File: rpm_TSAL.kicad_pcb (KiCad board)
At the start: 2 copper layers, 75.6 x 66.3 mm, 7 parts, among them J1 Conn_01x02, J2 Conn_01x02, J3 Conn_01x02, J4 Conn_01x02, U1 ADUM5202WCRWZ, U2 ADUM5202WCRWZ

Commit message: Saved. Initial Structure done.
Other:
- board size 75.6 x 66.3 mm -> 75.6 x 85 mm
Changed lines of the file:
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@@
 	(gr_rect
 		(start 47.425 59.325)
-		(end 123.025 125.625)
+		(end 123.025 144.325)
 		(stroke
 			(width 0.05)

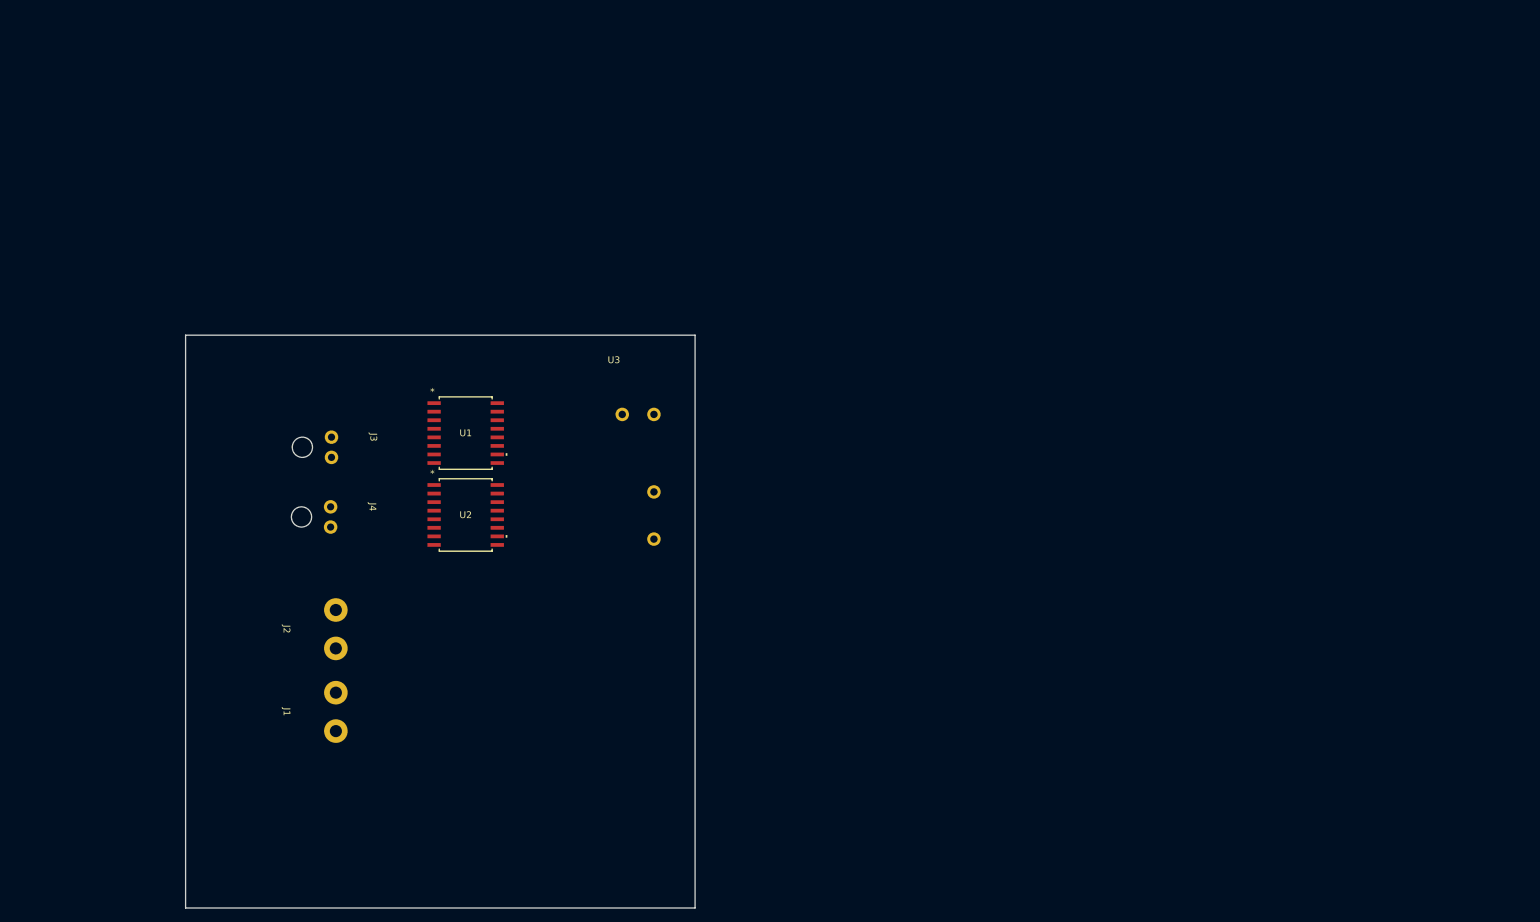
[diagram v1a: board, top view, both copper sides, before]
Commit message: Changes to Pinout pending
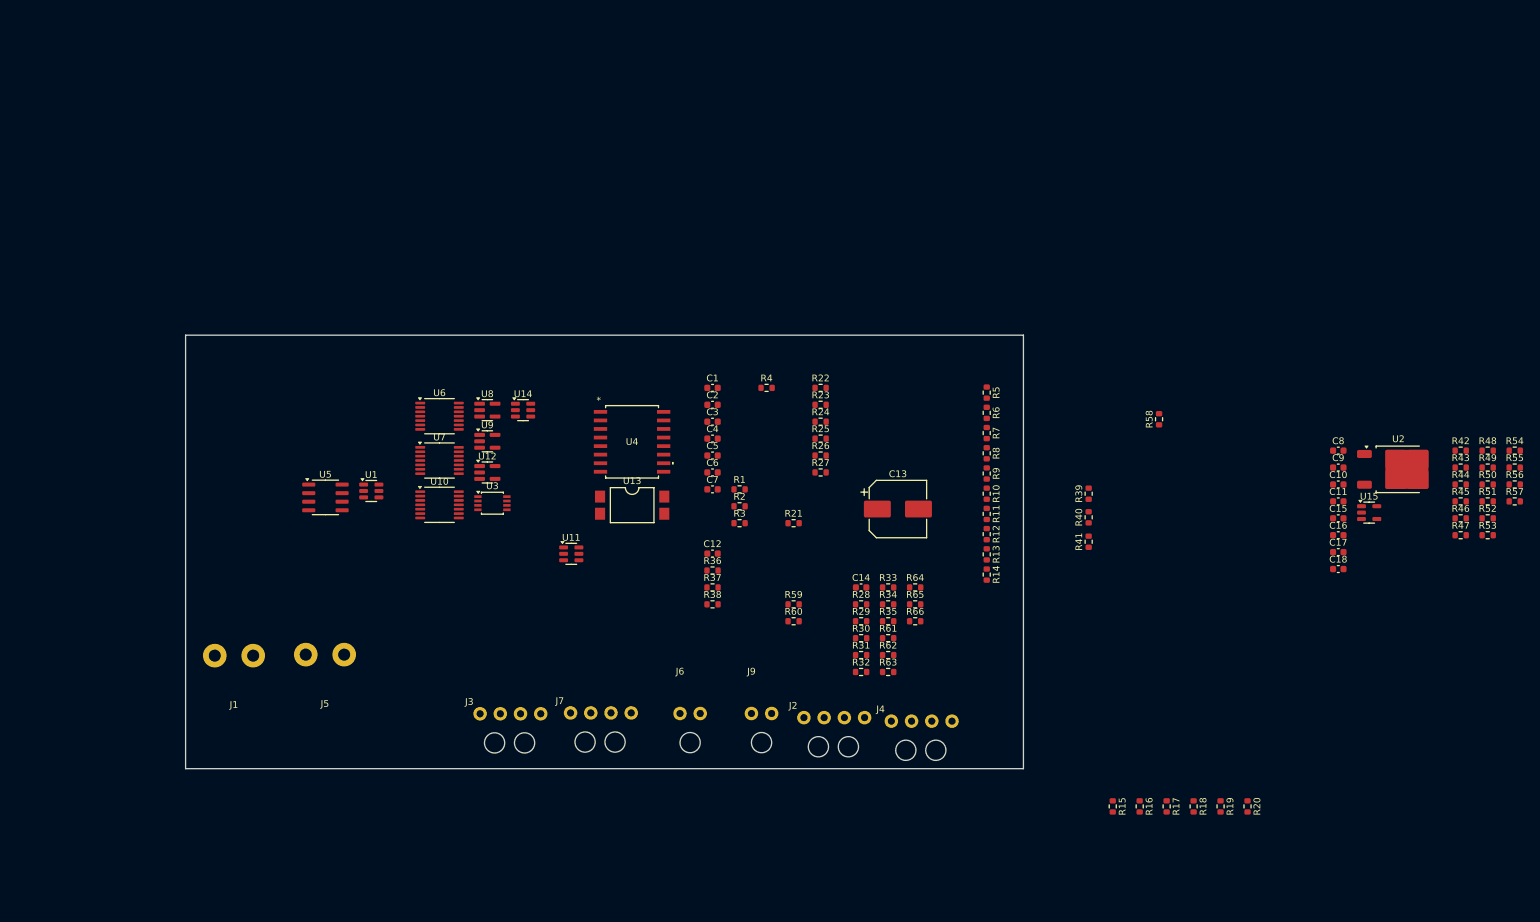
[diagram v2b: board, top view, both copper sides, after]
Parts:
- added C1: 100nF, Capacitor_SMD:C_0603_1608Metric, F.Cu at (125.6, 67.1)
- added C10: 100nF, Capacitor_SMD:C_0603_1608Metric, F.Cu at (218.5, 81.5)
- added C11: 100nF, Capacitor_SMD:C_0603_1608Metric, F.Cu at (218.5, 84.0)
- added C12: 100nF, Capacitor_SMD:C_0603_1608Metric, F.Cu at (125.6, 91.7)
- added C13: C_Polarized, Capacitor_SMD:CP_Elec_8x5.4, F.Cu at (153.1, 85.1)
- added C14: C, Capacitor_SMD:C_0603_1608Metric, F.Cu at (147.7, 96.8)
- added C15: 100nF, Capacitor_SMD:C_0603_1608Metric, F.Cu at (218.5, 86.5)
- added C16: 100nF, Capacitor_SMD:C_0603_1608Metric, F.Cu at (218.5, 89.0)
- added C17: 10uF, Capacitor_SMD:C_0603_1608Metric, F.Cu at (218.5, 91.5)
- added C18: 10uF, Capacitor_SMD:C_0603_1608Metric, F.Cu at (218.5, 94.0)
- added C2: 10uF, Capacitor_SMD:C_0603_1608Metric, F.Cu at (125.6, 69.7)
- added C3: 10uF, Capacitor_SMD:C_0603_1608Metric, F.Cu at (125.6, 72.2)
- added C4: 100nF, Capacitor_SMD:C_0603_1608Metric, F.Cu at (125.6, 74.7)
- added C5: 100nF, Capacitor_SMD:C_0603_1608Metric, F.Cu at (125.6, 77.2)
- added C6: 100nF, Capacitor_SMD:C_0603_1608Metric, F.Cu at (125.6, 79.7)
- added C7: 100nF, Capacitor_SMD:C_0603_1608Metric, F.Cu at (125.6, 82.2)
- added C8: 10uF, Capacitor_SMD:C_0603_1608Metric, F.Cu at (218.5, 76.5)
- added C9: 10uF, Capacitor_SMD:C_0603_1608Metric, F.Cu at (218.5, 79.0)
- added J5: Conn_01x02, wuerth_conn:657002130101, F.Cu at (65.3, 106.7)
- added J6: Conn_01x02, wuerth_conn:66200211024, F.Cu at (120.8, 115.5)
- added J7: Conn_01x04, wuerth_conn:66200411022, F.Cu at (103.0, 114.1)
- added J9: Conn_01x02, wuerth_conn:66200211024, F.Cu at (131.4, 115.5)
- added R1: 1k, Resistor_SMD:R_0603_1608Metric, F.Cu at (129.6, 82.2)
- added R10: 10k, Resistor_SMD:R_0603_1608Metric, F.Cu at (166.3, 82.8)
- added R11: 10k, Resistor_SMD:R_0603_1608Metric, F.Cu at (166.3, 85.8)
- added R12: 10k, Resistor_SMD:R_0603_1608Metric, F.Cu at (166.3, 88.8)
- added R13: 10k, Resistor_SMD:R_0603_1608Metric, F.Cu at (166.3, 91.8)
- added R14: 10k, Resistor_SMD:R_0603_1608Metric, F.Cu at (166.3, 94.8)
- added R15: 10k, Resistor_SMD:R_0603_1608Metric, F.Cu at (185.0, 129.2)
- added R16: 10k, Resistor_SMD:R_0603_1608Metric, F.Cu at (189.0, 129.2)
- added R17: 10k, Resistor_SMD:R_0603_1608Metric, F.Cu at (193.0, 129.2)
- added R18: 10k, Resistor_SMD:R_0603_1608Metric, F.Cu at (197.0, 129.2)
- added R19: 10k, Resistor_SMD:R_0603_1608Metric, F.Cu at (201.0, 129.2)
- added R2: 10k, Resistor_SMD:R_0603_1608Metric, F.Cu at (129.6, 84.7)
- added R20: 10k, Resistor_SMD:R_0603_1608Metric, F.Cu at (205.0, 129.2)
- added R21: 10k, Resistor_SMD:R_0603_1608Metric, F.Cu at (137.6, 87.2)
- added R22: 1k, Resistor_SMD:R_0603_1608Metric, F.Cu at (141.7, 67.1)
- added R23: 1k, Resistor_SMD:R_0603_1608Metric, F.Cu at (141.7, 69.7)
- added R24: 12k, Resistor_SMD:R_0603_1608Metric, F.Cu at (141.7, 72.2)
- added R25: 1k, Resistor_SMD:R_0603_1608Metric, F.Cu at (141.7, 74.7)
- added R26: 1k, Resistor_SMD:R_0603_1608Metric, F.Cu at (141.7, 77.2)
- added R27: 10k, Resistor_SMD:R_0603_1608Metric, F.Cu at (141.7, 79.7)
- added R28: 10k, Resistor_SMD:R_0603_1608Metric, F.Cu at (147.7, 99.3)
- added R29: 10k, Resistor_SMD:R_0603_1608Metric, F.Cu at (147.7, 101.8)
- added R3: 10k, Resistor_SMD:R_0603_1608Metric, F.Cu at (129.6, 87.2)
- added R30: 10k, Resistor_SMD:R_0603_1608Metric, F.Cu at (147.7, 104.3)
- added R31: 3k3, Resistor_SMD:R_0603_1608Metric, F.Cu at (147.7, 106.8)
- added R32: 3k3, Resistor_SMD:R_0603_1608Metric, F.Cu at (147.7, 109.3)
- added R33: 3k3, Resistor_SMD:R_0603_1608Metric, F.Cu at (151.7, 96.8)
- added R34: 10k, Resistor_SMD:R_0603_1608Metric, F.Cu at (151.7, 99.3)
- added R35: 200R, Resistor_SMD:R_0603_1608Metric, F.Cu at (151.7, 101.8)
- added R36: 12k, Resistor_SMD:R_0603_1608Metric, F.Cu at (125.6, 94.2)
- added R37: 1k, Resistor_SMD:R_0603_1608Metric, F.Cu at (125.6, 96.8)
- added R38: 1k, Resistor_SMD:R_0603_1608Metric, F.Cu at (125.6, 99.3)
- added R39: 10k, Resistor_SMD:R_0603_1608Metric, F.Cu at (181.4, 82.8)
- added R4: 10k, Resistor_SMD:R_0603_1608Metric, F.Cu at (133.6, 67.1)
- added R40: 10k, Resistor_SMD:R_0603_1608Metric, F.Cu at (181.4, 86.3)
- added R41: 10k, Resistor_SMD:R_0603_1608Metric, F.Cu at (181.4, 90.0)
- added R42: 10k, Resistor_SMD:R_0603_1608Metric, F.Cu at (236.6, 76.5)
- added R43: 10k, Resistor_SMD:R_0603_1608Metric, F.Cu at (236.6, 79.0)
- added R44: 10k, Resistor_SMD:R_0603_1608Metric, F.Cu at (236.6, 81.5)
- added R45: 10k, Resistor_SMD:R_0603_1608Metric, F.Cu at (236.6, 84.0)
- added R46: 10k, Resistor_SMD:R_0603_1608Metric, F.Cu at (236.6, 86.5)
- added R47: 10k, Resistor_SMD:R_0603_1608Metric, F.Cu at (236.6, 89.0)
- added R48: 10k, Resistor_SMD:R_0603_1608Metric, F.Cu at (240.6, 76.5)
- added R49: 10k, Resistor_SMD:R_0603_1608Metric, F.Cu at (240.6, 79.0)
- added R5: 10k, Resistor_SMD:R_0603_1608Metric, F.Cu at (166.3, 67.8)
- added R50: 10k, Resistor_SMD:R_0603_1608Metric, F.Cu at (240.6, 81.5)
- added R51: 10k, Resistor_SMD:R_0603_1608Metric, F.Cu at (240.6, 84.0)
- added R52: 10k, Resistor_SMD:R_0603_1608Metric, F.Cu at (240.6, 86.5)
- added R53: 10k, Resistor_SMD:R_0603_1608Metric, F.Cu at (240.6, 89.0)
- added R54: 10k, Resistor_SMD:R_0603_1608Metric, F.Cu at (244.7, 76.5)
- added R55: 10k, Resistor_SMD:R_0603_1608Metric, F.Cu at (244.7, 79.0)
- added R56: 10k, Resistor_SMD:R_0603_1608Metric, F.Cu at (244.7, 81.5)
- added R57: 10k, Resistor_SMD:R_0603_1608Metric, F.Cu at (244.7, 84.0)
- added R58: 10k, Resistor_SMD:R_0603_1608Metric, F.Cu at (191.9, 71.8)
- added R59: 1k, Resistor_SMD:R_0603_1608Metric, F.Cu at (137.6, 99.3)
- added R6: 10k, Resistor_SMD:R_0603_1608Metric, F.Cu at (166.3, 70.8)
- added R60: 1k, Resistor_SMD:R_0603_1608Metric, F.Cu at (137.6, 101.8)
- added R61: 10k, Resistor_SMD:R_0603_1608Metric, F.Cu at (151.7, 104.3)
- added R62: 10k, Resistor_SMD:R_0603_1608Metric, F.Cu at (151.7, 106.8)
- added R63: 33k, Resistor_SMD:R_0603_1608Metric, F.Cu at (151.7, 109.3)
- added R64: 33k, Resistor_SMD:R_0603_1608Metric, F.Cu at (155.7, 96.8)
- added R65: 10k, Resistor_SMD:R_0603_1608Metric, F.Cu at (155.7, 99.3)
- added R66: 10k, Resistor_SMD:R_0603_1608Metric, F.Cu at (155.7, 101.8)
- added R7: 10k, Resistor_SMD:R_0603_1608Metric, F.Cu at (166.3, 73.8)
- added R8: 10k, Resistor_SMD:R_0603_1608Metric, F.Cu at (166.3, 76.8)
- added R9: 10k, Resistor_SMD:R_0603_1608Metric, F.Cu at (166.3, 79.8)
- added U10: SN74HCS266PWR, Package_SO:TSSOP-14_4.4x5mm_P0.65mm, F.Cu at (85.1, 84.5)
- added U11: OPA355NA, Package_TO_SOT_SMD:SOT-23-6, F.Cu at (104.7, 91.8)
- added U12: 74LVC1G32GV, Package_SO:SC-74A-5_1.55x2.9mm_P0.95mm, F.Cu at (92.2, 79.7)
- added U13: SFH617A-1X007T, Package_DIP:SMDIP-4_W9.53mm_Clearance8mm, F.Cu at (113.7, 84.5)
- added U14: OPA355NA, Package_TO_SOT_SMD:SOT-23-6, F.Cu at (97.5, 70.5)
- added U15: ADP121-AUJZ33R7, Package_TO_SOT_SMD:TSOT-23-5, F.Cu at (223.1, 85.7)
- added U4: ADUM5202WCRWZ, ADUM5202:RW_16_ADI, F.Cu at (113.7, 75.2)
- added U5: NE555D, Package_SO:SOIC-8_3.9x4.9mm_P1.27mm, F.Cu at (68.2, 83.4)
- added U6: CD74HC30PWR, Package_SO:TSSOP-14_4.4x5mm_P0.65mm, F.Cu at (85.1, 71.3)
- added U7: 4072, Package_SO:TSSOP-14_4.4x5mm_P0.65mm, F.Cu at (85.1, 77.9)
- added U8: 4001, Package_SO:SC-74A-5_1.55x2.9mm_P0.95mm, F.Cu at (92.2, 70.5)
- added U9: 74LVC1G32GV, Package_SO:SC-74A-5_1.55x2.9mm_P0.95mm, F.Cu at (92.2, 75.1)
- J2: value Conn_01x02 -> Conn_01x04; footprint wuerth_conn:657002130101 -> wuerth_conn:66200411022
- J3, J4: value Conn_01x02 -> Conn_01x04; footprint wuerth_conn:66200211024 -> wuerth_conn:66200411022
- U1: value ADUM5202WCRWZ -> OPA355NA; footprint ADUM5202:RW_16_ADI -> Package_TO_SOT_SMD:SOT-23-6
- U2: value ADUM5202WCRWZ -> L7805; footprint ADUM5202:RW_16_ADI -> Package_TO_SOT_SMD:TO-252-2
- U3: value ~ -> 74LVC2G74; footprint Zettler:AZ9371 -> Package_SO:TSSOP-8_3x3mm_P0.65mm
- moved U2 138.6 mm to (227.4, 79.2)
- moved J4 87.1 mm to (150.6, 115.3), turned to 0 degrees
- moved J2 69.4 mm to (137.6, 114.8), turned to 0 degrees
- moved J3 44.7 mm to (89.5, 114.2), turned to 0 degrees
- moved U3 22.9 mm to (93.0, 84.3)
- moved J1 18.8 mm to (51.8, 106.9), turned to 0 degrees
- moved U1 16.4 mm to (75.0, 82.4)
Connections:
- J2 pad 1:  HV_{ACCU+} -> /LV_Connectors/PRCH_Coil
- J2 pad 2: HV_{ACCU-} -> GND
- J3 pad 1: unconnected-(J3-Pin_1-Pad1) -> /LV_Connectors/AIR1_Coil
- J3 pad 2: unconnected-(J3-Pin_2-Pad2) -> GND
- J4 pad 1: unconnected-(J4-Pin_1-Pad1) -> /LV_Connectors/AIR2_Coil
- J4 pad 2: unconnected-(J4-Pin_2-Pad2) -> GND
- U1 pad 1: unconnected-(U1-VDD1-Pad1) -> Net-(U4-VIA)
- U1 pad 2: unconnected-(U1-GND1-Pad2) -> HV_RED-
- U1 pad 3: unconnected-(U1-VOA-Pad3) -> Net-(U1-+)
- U1 pad 4: unconnected-(U1-VOB-Pad4) -> Net-(U1--)
- U1 pad 5: unconnected-(U1-RCIN-Pad5) -> +5V_{iso}
- U1 pad 6: unconnected-(U1-RCSEL-Pad6) -> +5V_{iso}
- U2 pad 1: unconnected-(U2-VDD1-Pad1) -> +12V
- U2 pad 2: unconnected-(U2-GND1-Pad2) -> GND
- U2 pad 3: unconnected-(U2-VOA-Pad3) -> +5V
- U3 pad 1: unconnected-(U3-Coil_B-Pad1) -> GND
- U3 pad 5: unconnected-(U3-SW2-Pad5) -> /TSAL_Plausibility/TSAL_ERROR
- U3 pad 7: unconnected-(U3-SW1-Pad7) -> Net-(U3-~{S})
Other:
- board size 75.6 x 85 mm -> 124.3 x 64.3 mm

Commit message: Checked Rules. Looks good. Need to fix AIR Aux detection. Need to Fix Coil Activation. Need to add SCS Failure Output and SCS Failure Inhibiter
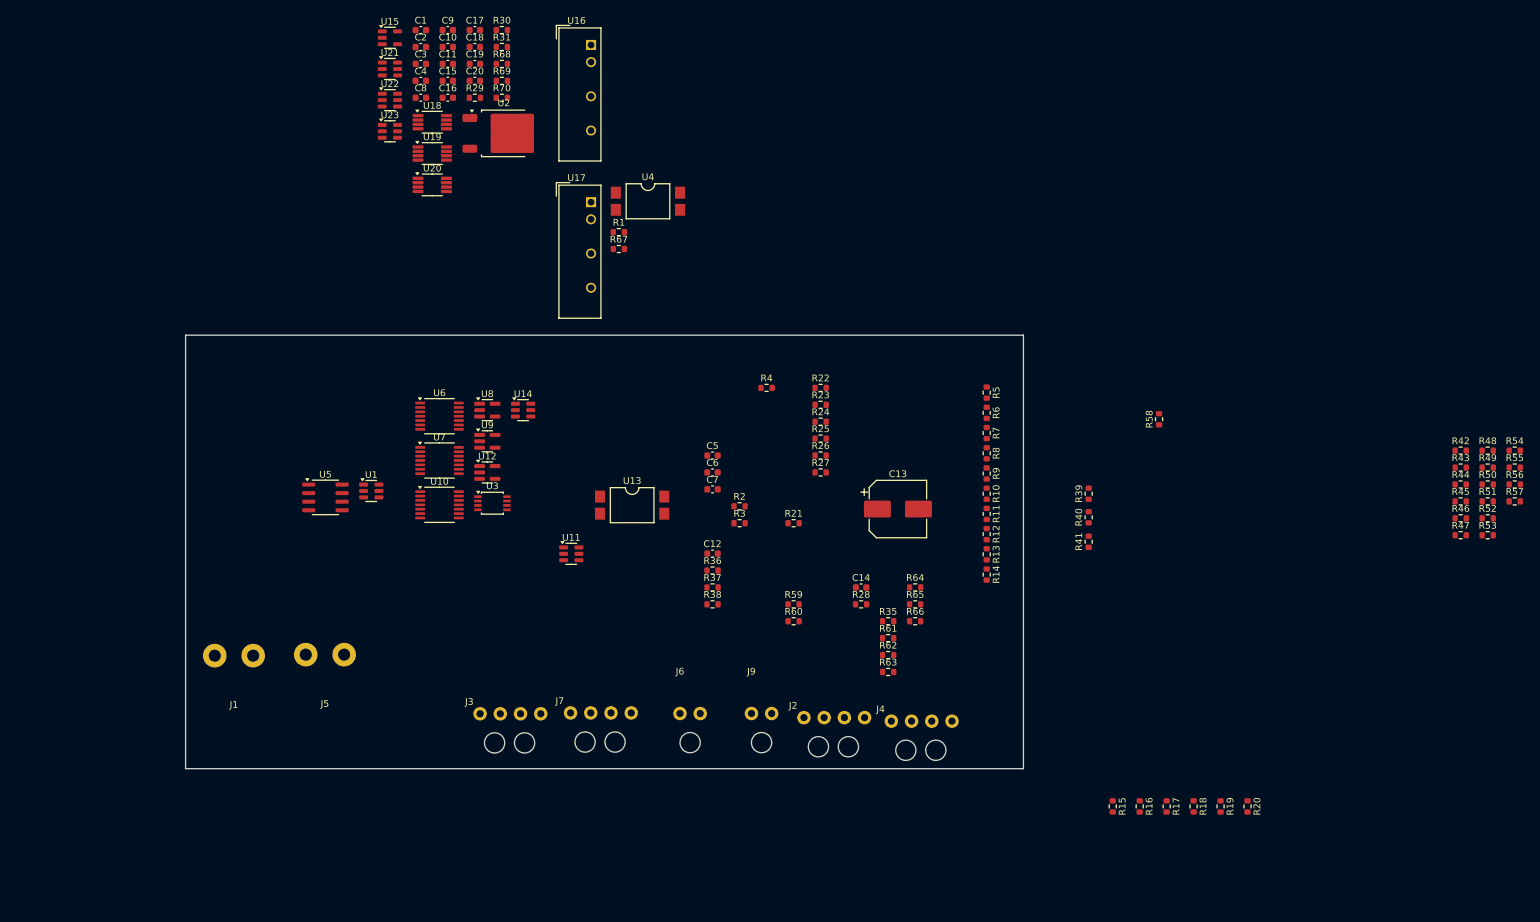
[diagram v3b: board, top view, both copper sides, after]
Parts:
- removed R32, R33: 3k3, Resistor_SMD:R_0603_1608Metric
- removed R34: 10k, Resistor_SMD:R_0603_1608Metric
- added C19: 100nF, Capacitor_SMD:C_0603_1608Metric, F.Cu at (90.3, 19.1)
- added C20: 100nF, Capacitor_SMD:C_0603_1608Metric, F.Cu at (90.3, 21.6)
- added R67: 1k, Resistor_SMD:R_0603_1608Metric, F.Cu at (111.7, 46.5)
- added R68: 200k, Resistor_SMD:R_0603_1608Metric, F.Cu at (94.4, 19.1)
- added R69: 200k, Resistor_SMD:R_0603_1608Metric, F.Cu at (94.4, 21.6)
- added R70: 200k, Resistor_SMD:R_0603_1608Metric, F.Cu at (94.4, 24.1)
- added U16: TBA1-0511E, Converter_DCDC:Converter_DCDC_TRACO_TBA1-xxxxE_Single_THT, F.Cu at (107.6, 16.3)
- added U17: TBA1-0511E, Converter_DCDC:Converter_DCDC_TRACO_TBA1-xxxxE_Single_THT, F.Cu at (107.6, 39.6)
- added U18: LM393ADGKR, Package_SO:VSSOP-8_3x3mm_P0.65mm, F.Cu at (84.0, 27.7)
- added U19: LM393ADGKR, Package_SO:VSSOP-8_3x3mm_P0.65mm, F.Cu at (84.0, 32.4)
- added U20: LM393ADGKR, Package_SO:VSSOP-8_3x3mm_P0.65mm, F.Cu at (84.0, 37.0)
- added U21: OPA355NA, Package_TO_SOT_SMD:SOT-23-6, F.Cu at (77.7, 19.8)
- added U22: OPA355NA, Package_TO_SOT_SMD:SOT-23-6, F.Cu at (77.7, 24.4)
- added U23: OPA355NA, Package_TO_SOT_SMD:SOT-23-6, F.Cu at (77.7, 29.1)
- C11, C15: value 100nF -> 10uF
- C17, C18, C8, C9: value 10uF -> 100nF
- R31: value 3k3 -> 10k
- U4: value ADUM5202WCRWZ -> SFH617A-1X007T; footprint ADUM5202:RW_16_ADI -> Package_DIP:SMDIP-4_W9.53mm_Clearance8mm
- moved U15 161.5 mm to (77.7, 15.2)
- moved C17 149.7 mm to (90.3, 14.1)
- moved C18 149.7 mm to (90.3, 16.6)
- moved C10 147.2 mm to (86.3, 16.6)
- moved C16 147.2 mm to (86.3, 24.1)
- moved C11 147.2 mm to (86.3, 19.1)
- moved C15 147.2 mm to (86.3, 21.6)
- moved C9 147.2 mm to (86.3, 14.1)
- moved C8 145.9 mm to (82.3, 24.1)
- moved U2 141.8 mm to (94.6, 29.4)
- moved R31 104.8 mm to (94.4, 16.6)
- moved R30 104.8 mm to (94.4, 14.1)
- moved R29 96.5 mm to (90.3, 24.1)
- moved C1 68.5 mm to (82.3, 14.1)
- moved C2 68.5 mm to (82.3, 16.6)
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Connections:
- net /LV_Connectors/SC_Sense renamed /LV_Connectors/SC
- C10 pad 1: +5V -> +3V3
- C11 pad 1: +12V -> +5V
- C15 pad 1: +5V -> +3V3
- C16 pad 1: +3V3 -> +5V
- C18 pad 1: +3V3 -> /LV_Connectors/AIR2_AUX
- C3 pad 1: +5V_{iso} -> +12V
- C3 pad 2: HV_RED- -> GND
- C4 pad 1: +5V_{iso} -> +5V
- C4 pad 2: HV_RED- -> GND
- C5 pad 1: +5V_{iso} -> +5V_{iso_RED}
- C8 pad 1: +5V -> +12V
- C9 pad 1: +12V -> +5V
- J2 pad 2: GND -> unconnected-(J2-Pin_2-Pad2)
- J2 pad 3: /LV_Connectors/PRCH_AUX -> /LV_Connectors/PRCH_Coil_unbuffered
- J3 pad 2: GND -> unconnected-(J3-Pin_2-Pad2)
- J3 pad 3: /LV_Connectors/AIR1_AUX -> /LV_Connectors/AIR1_AUX_unbuffered
- J4 pad 2: GND -> unconnected-(J4-Pin_2-Pad2)
- J4 pad 3: /LV_Connectors/AIR2_AUX -> /LV_Connectors/AIR1_AUX_unbuffered
- R1 pad 1: Net-(U4-VIB) -> GND
- R1 pad 2: HV_RED- -> Net-(U5-R)
- R24 pad 2: +5V_{iso} -> +5V_{iso_RED}
- R29 pad 1: /LV_Connectors/AIR2_Coil -> /LV_Connectors/AIR2_AUX
- R29 pad 2: Net-(R29-Pad2) -> +5V
- R30 pad 1: /LV_Connectors/PRCH_Coil -> /LV_Connectors/AIR1_AUX
- R30 pad 2: Net-(R30-Pad2) -> +5V
- R31 pad 1: GND -> /LV_Connectors/PRCH_AUX
- R31 pad 2: Net-(R31-Pad2) -> +5V
- U1 pad 1: Net-(U4-VIA) -> Net-(U1-Pad1)
- U1 pad 5: +5V_{iso} -> +5V_{iso_RED}
- U1 pad 6: +5V_{iso} -> +5V_{iso_RED}
- U10 pad 2: Net-(R31-Pad2) -> /LV_Connectors/AIR1_Coil
- U10 pad 6: Net-(R29-Pad2) -> /LV_Connectors/AIR2_Coil
- U10 pad 9: Net-(R30-Pad2) -> /LV_Connectors/PRCH_Coil
- U4 pad 1: +5V -> Net-(U1-Pad1)
- U4 pad 2: GND -> Net-(R67-Pad2)
- U4 pad 3: Net-(U4-VOA) -> Net-(U5-R)
- U4 pad 4: unconnected-(U4-VOB-Pad4) -> +5V
- U5 pad 4: Net-(U4-VOA) -> Net-(U5-R)

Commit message: ⠀⠀⠀⠀⠀⠀⠀⠀⠀⠀⠀⠀⠀⠀⠀⠀⠀⠀⠀⠀⠀⠀⠀⠀⠀⠀⠀⠀⠀⠀⠀⠀⠀⠀⠀⠀⠀⣠⣤⣤⣤⡀⠀⠀⠀⠀⠀⠀⠀⠀⠀⠀⠀⠀⠀⠀⠀⠀⠀⠀⠀⠀⠀⠀⠀ ⠀⠀⠀⠀⠀⠀⠀⠀⠀⠀⠀⠀⠀⠀⠀⠀⠀⠀⠀⠀⠀⠀⠀⠀⠀⠀⠀⠀⠀⠀⠀⠀⠀⠀⣠⣶⣿⠟⠉⠉⠻⣿⡄⠀⠀⠀⠀⠀⠀⠀⠀⠀⠀⠀⠀⠀⠀⠀⠀⠀⠀⠀⠀⠀⠀ ⠀⠀⠀⠀⠀⠀⠀⠀⠀⠀⠀⠀⠀⠀⠀⠀⠀⠀⠀⠀⠀⠀⠀⠀⠀⠀⠀⠀⠀⠀⠀⢀⣤⣾⠿⠉⠀⠀⠀⠀⠀⠹⣿⡄⠀⠀⠀⠀⠀⠀⠀⠀⠀⠀⠀⠀⠀⠀⠀⠀⠀⠀⣀⣴⣾ ⠀⠀⠀⠀⠀⠀⠀⠀⠀⠀⠀⠀⠀⠀⠀⠀⠀⠀⠀⠀⠀⠀⠀⠀⠀⠀⠀⠀⠀⢀⣴⣿⠟⠁⠀⠀⠀⠀⠀⠀⠀⠀⣿⣿⠀⠀⠀⠀⠀⠀⠀⠀⠀⠀⠀⠀⠀⠀⠀⣀⣴⣾⡿⠛⠉ ⠀⠀⠀⠀⠀⠀⠀⠀⠀⠀⠀⠀⠀⠀⠀⠀⠀⠀⠀⠀⠀⠀⠀⠀⠀⠀⠀⢀⣴⣿⠟⠁⠀⠀⠀⠀⠀⠀⠀⠀⠀⠀⢸⣿⡆⠀⠀⠀⠀⠀⠀⠀⠀⠀⠀⠀⢀⣴⣾⡿⠟⠁⠀⠀⠀ ⠀⠀⠀⠀⠀⠀⠀⠀⠀⠀⠀⠀⠀⠀⠀⠀⠀⠀⠀⠀⠀⠀⠀⠀⢀⣀⣴⣿⡿⠃⠀⠀⠀⠀⠀⠀⠀⠀⠀⠀⠀⠀⢸⣿⣷⣶⣶⣦⣤⣤⣄⡀⠀⢀⣠⣾⣿⠿⠋⠀⠀⠀⠀⠀⣠ ⠀⠀⠀⠀⠀⠀⠀⠀⠀⠀⠀⠀⠀⠀⠀⠀⠀⠀⠀⠀⠀⠀⠀⣼⣿⣿⡿⠋⠀⠀⠀⠀⠀⠀⠀⠀⠀⠀⠀⣠⣤⠶⠞⣿⠟⠋⠉⠉⠙⣻⠿⢿⣿⣿⣿⠟⠁⠀⠀⠀⠀⠀⢀⡼⠁ ⠀⠀⠀⠀⠀⠀⠀⠀⠀⠀⠀⠀⠀⠀⠀⠀⠀⠀⠀⠀⠀⠀⢰⣿⠁⠛⠀⠀⠀⠀⠀⠀⠀⠀⠀⠀⠀⠀⣰⠟⠁⢠⡞⠁⠀⠀⠀⢀⡴⠋⠀⢀⡿⠋⠁⠀⠀⠀⠀⠀⠀⠀⡞⠁⠀ ⠀⠀⠀⠀⠀⠀⠀⠀⠀⠀⠀⠀⠀⠀⠀⠀⠀⠀⠀⠀⠀⣠⣼⣿⡄⠀⠀⠀⠀⠀⠀⠀⠀⠀⠀⠀⠀⣼⠃⠀⢠⠏⠀⠀⠀⠀⣰⠏⠀⠀⣠⠟⠀⠀⠀⠀⠀⠀⠀⠀⠀⢸⡥⠤⡀ ⠀⠀⠀⠀⠀⠀⠀⠀⠀⠀⠀⠀⠀⠀⠀⠀⠀⠀⠀⠀⣰⣿⠟⠁⠀⠀⠀⠀⠀⠀⠀⠀⠀⠀⠀⠀⠠⣇⠀⣠⡏⠀⠀⠀⠀⣼⠁⠀⠀⣰⠋⠀⠀⠀⠀⠀⠀⠀⠀⠀⠀⠀⢀⡴⠁ ⠀⠀⠀⠀⠀⠀⠀⠀⠀⠀⠀⠀⠀⠀⠀⠀⣀⣄⣄⣼⣿⠋⠀⠀⠀⠀⠀⠀⠀⠀⠀⠀⠀⠀⠀⠀⠀⢻⡶⠋⠀⠀⠀⠀⢸⣧⠀⠀⣴⠃⠀⠀⠀⠀⠀⠀⠀⠀⠀⠀⠀⠀⠘⢧⠀ ⠀⠀⠀⠀⠀⠀⠀⠀⢀⣀⣀⠀⠀⠀⠀⣾⡿⠿⣿⡿⠁⠀⠀⠀⠀⠀⠀⣠⣶⣶⣶⡀⠀⠀⠀⠀⠀⠀⠀⠀⠀⠀⠀⠀⠀⠙⠛⠛⠁⠀⠀⠀⠀⠀⠀⠀⠀⠀⠀⠀⠀⠀⠀⠈⠳ ⠀⠀⠀⠀⠀⠀⢀⣾⠿⠛⢿⣿⣷⣄⡀⣿⠃⠀⠈⠀⠀⠀⠀⠀⠀⢀⣾⣿⣿⣿⣿⣧⠀⠀⠀⠀⠀⠀⠀⠀⠀⠀⠀⠀⠀⠀⠀⠀⠀⠀⠀⠀⠀⠀⠀⠀⠀⠀⠀⠀⠀⠀⠀⠀⠀ ⠀⠀⠀⣠⣤⣦⣼⣿⠀⠀⠀⣿⣿⣿⣿⣿⣦⣀⠀⠀⠀⠀⠀⠀⠀⣿⣿⣿⣿⣿⣿⡿⠀⠀⠀⢀⣀⣀⣀⣀⡀⠀⠀⠀⠀⠀⠀⠀⠀⠀⠀⣤⣾⣿⣿⣿⣷⣄⠀⠀⠀⠀⠀⠀⠀ ⠀⣠⣾⡿⠋⠉⠉⠁⠀⠀⠀⠀⠉⢯⡙⠻⣿⣿⣷⣤⡀⠀⠀⠀⠀⢿⣿⣿⣿⣿⡿⠃⢀⡤⠖⠋⠉⠉⠉⠉⠉⠉⠒⠦⣄⠀⠀⠀⠀⠀⣾⣿⣿⣿⣿⣿⣿⣿⣧⠀⠀⠀⠀⠀⠀ ⣾⣿⠋⠀⠀⠀⠀⣀⣀⠀⠀⠀⠀⠀⠙⢦⣄⠉⠻⢿⣿⣷⣦⡀⠀⠈⠙⠛⠛⠋⠀⢰⠟⡇⠀⠀⠀⠀⠀⠀⠀⠀⠀⠀⠈⠳⣄⠀⠀⠀⣿⣿⣿⣿⣿⣿⣿⣿⣿⠀⠀⠀⠀⠀⠀ ⣿⡇⠀⠀⠀⣴⠟⣫⣿⣿⣄⠀⠀⠀⠀⡶⢌⡙⠶⣤⡈⠛⠿⣿⣷⣦⣀⠀⠀⠀⠀⡇⠀⢻⣄⠀⠀⣠⢷⠀⠀⠀⠀⠀⡶⠀⠘⡆⠀⠀⠻⣿⣿⣿⣿⣿⣿⣿⡟⠀⠀⠀⠀⠀⠀ ⣿⡇⠀⠀⢸⣟⢸⣿⣿⣿⣿⠀⠀⠀⠀⡇⠀⠈⠛⠦⣝⡳⢤⣈⠛⠻⣿⣷⣦⣀⠀⠀⠀⠀⠈⠙⠋⠁⠀⠛⠦⠤⠤⠚⠁⠀⠀⢳⠀⠀⠀⠈⠛⠿⠿⠿⠟⠋⠀⠀⠀⠀⠀⠀⠀ ⣿⡇⠀⠀⠈⢿⣞⣿⣿⣿⠏⠀⠀⠀⠀⡇⠀⠀⠀⠀⠀⠙⠳⢬⣛⠦⠀⠙⢻⣿⣷⣦⣀⠀⠀⠀⠀⠀⠀⠀⠀⠀⠀⠀⠀⠀⠀⡞⠀⠀⠀⠀⠀⠀⠀⠀⠀⠀⠀⠀⠀⠀⠀⠀⠀ ⣿⡇⠀⠀⠀⠀⠉⠛⠋⠁⠀⠀⠀⠀⠀⡇⠀⠀⠀⠀⠀⠀⠀⠀⠈⠁⠀⠀⠈⣿⠉⢻⣿⣷⣦⣀⠀⠀⠀⠀⠀⠀⠀⠀⠀⢀⡼⠁⠀⠀⠀⠀⠀⠀⠀⠀⠀⠀⠀⠀⠀⠀⠀⠀⠀ ⣿⡇⠀⠀⠀⠀⠀⣠⣄⠀⠀⢰⠶⠒⠒⢧⣄⡀⠀⠀⠀⠀⠀⠀⠀⠀⠀⠀⠀⣿⠀⢸⡇⢸⡟⢿⣷⣦⣴⣶⣶⣶⣶⣤⣔⠋⠀⠀⠀⠀⠀⠀⠀⠀⠀⠀⠀⠀⠀⠀⠀⠀⠀⠀⠀ ⣿⡇⠀⠀⣤⠀⠀⠿⠿⠁⢀⡿⠀⠀⠀⡄⠈⠙⡷⢦⣄⡀⠀⠀⠀⠀⠀⠀⠀⣿⠀⢸⡇⢸⡇⠀⣿⠙⣿⣿⣉⠉⠙⠿⣿⣧⠀⠀⠀⠀⠀⠀⠀⠀⠀⠀⠀⠀⠀⠀⠀⠀⠀⠀⠀ ⣿⡇⠀⠀⠙⠷⢤⣀⣠⠴⠛⠁⠀⠀⠀⠇⠀⠀⡇⢸⡏⢹⡷⢦⣄⡀⠀⠀⠀⣿⡀⢸⡇⢸⡇⠀⡟⠀⢸⠀⢹⡷⢦⣄⣘⣿⡆⠀⠀⠀⠀⠀⠀⠀⠀⠀⠀⠀⠀⠀⠀⠀⠀⠀⠀ ⣿⣿⠢⣤⡀⠀⠀⠀⠀⠀⠀⣠⠾⣿⣿⡷⣤⣀⡇⠸⡇⢸⡇⢸⠉⠙⠳⢦⣄⡻⢿⣾⣧⣸⣧⠀⡇⠀⢸⠀⢸⡇⢤⣈⠙⠻⣿⣆⠀⠀⠀⠀⠀⠀⠀⠀⠀⠀⠀⠀⠀⠀⠀⠀⠀ ⢹⣿⣷⣌⡉⠛⠲⢶⣶⠖⠛⠛⢶⣄⡉⠛⠿⣽⣿⣶⣧⣸⡇⢸⠀⠀⠀⠀⠈⠙⠲⢮⣝⠻⣿⣷⣷⣄⣸⠀⢸⡇⠀⠈⠁⠀⢸⣿⠀⠀⠀⠀⠀⠀⠀⠀⠀⠀⠀⠀⠀⠀⠀⠀⠀ ⠀⠈⠙⠻⢿⣷⣶⣤⣉⡻⢶⣄⣀⠈⠙⠳⢦⣈⡉⠻⢿⣿⣷⣾⣦⡀⠀⠀⠀⠀⠀⠀⠈⠙⠲⢭⣛⠿⣿⣷⣼⡇⠀⠀⠀⠀⠈⣿⡇⠀⠀⠀⠀⠀⠀⣀⠀⠀⠀⠀⠀⠀⠀⠀⣀ ⠀⠀⠀⠀⠀⠈⠙⠻⢿⣿⣷⣶⣽⣻⡦⠀⠀⠈⠙⠷⣦⣌⡙⠻⢿⣟⣷⣤⣀⠀⠀⠀⠀⠀⠀⠀⠈⠙⠳⢯⣻⡇⠀⠀⠀⠀⠀⢸⣿⠀⣀⠀⠀⠀⠀⠈⠳⣄⠀⠀⠀⢀⡏⠙⠛ ⠀⠀⠀⠀⠀⠀⠀⠀⠀⠈⠛⠻⢿⣿⣿⣿⣶⣤⣤⣤⣀⣈⠛⠷⣤⣈⡛⠷⢽⡻⢶⣄⣀⠀⠀⠀⠀⠀⠀⠀⠈⠛⠳⢤⣀⠀⠀⢸⣿⡀⠈⠳⢤⣀⣀⣰⠃⠈⠛⠶⠶⠿⠃⠀⠀ ⠀⠀⠀⠀⠀⠀⠀⠀⠀⠀⠀⠀⠀⢈⣿⡿⠛⠉⠙⠛⠛⠻⢷⣦⣄⣩⣿⠶⠖⠛⠛⠛⠛⠛⠛⠿⢷⣶⣦⣄⠀⠀⠀⠀⠉⢻⣶⣿⣿⠇⠀⠀⠀⠉⠉⠀⠀⠀⠀⠀⠀⠀⠀⠀⠀ ⠀⠀⠀⠀⠀⠀⠀⠀⠀⠀⠀⠀⠀⣼⣿⠁⠀⠀⠀⠀⠀⠀⠀⣿⣿⠋⠀⠀⠀⠀⠀⣠⠖⠂⠀⠀⠀⠈⠙⠿⣿⣦⡄⠀⠀⣸⣿⠟⠋⠀⠀⠀⠀⠀⠀⠀⠀⠀⠀⠀⠀⠀⠀⠀⠀ ⠀⠀⠀⠀⠀⠀⠀⠀⠀⠀⠀⠀⢰⣿⡟⠀⠀⠀⠀⠀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
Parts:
- removed C1, C10, C12, C16, C17, C18, C19, C20, C4, C5, C6, C7, C8, C9: 100nF, Capacitor_SMD:C_0603_1608Metric
- removed C11, C15, C2, C3: 10uF, Capacitor_SMD:C_0603_1608Metric
- removed C13: C_Polarized, Capacitor_SMD:CP_Elec_8x5.4
- removed C14: C, Capacitor_SMD:C_0603_1608Metric
- removed J1, J5: Conn_01x02, wuerth_conn:657002130101
- removed J2, J3, J4, J7: Conn_01x04, wuerth_conn:66200411022
- removed J6, J9: Conn_01x02, wuerth_conn:66200211024
- removed R1, R22, R23, R25, R26, R37, R38, R59, R60, R67: 1k, Resistor_SMD:R_0603_1608Metric
- removed R10, R11, R12, R13, R14, R15, R16, R17, R18, R19, R2, R20, R21, R27, R28, R29, R3, R30, R31, R39, R4, R40, R41, R42, R43, R44, R45, R46, R47, R48, R49, R5, R50, R51, R52, R53, R54, R55, R56, R57, R58, R6, R61, R62, R65, R66, R7, R8, R9: 10k, Resistor_SMD:R_0603_1608Metric
- removed R24, R36: 12k, Resistor_SMD:R_0603_1608Metric
- removed R35: 200R, Resistor_SMD:R_0603_1608Metric
- removed R63, R64: 33k, Resistor_SMD:R_0603_1608Metric
- removed R68, R69, R70: 200k, Resistor_SMD:R_0603_1608Metric
- removed U1, U11, U14, U21, U22, U23: OPA355NA, Package_TO_SOT_SMD:SOT-23-6
- removed U10: SN74HCS266PWR, Package_SO:TSSOP-14_4.4x5mm_P0.65mm
- removed U12, U9: 74LVC1G32GV, Package_SO:SC-74A-5_1.55x2.9mm_P0.95mm
- removed U13, U4: SFH617A-1X007T, Package_DIP:SMDIP-4_W9.53mm_Clearance8mm
- removed U15: ADP121-AUJZ33R7, Package_TO_SOT_SMD:TSOT-23-5
- removed U16, U17: TBA1-0511E, Converter_DCDC:Converter_DCDC_TRACO_TBA1-xxxxE_Single_THT
- removed U18, U19, U20: LM393ADGKR, Package_SO:VSSOP-8_3x3mm_P0.65mm
- removed U2: L7805, Package_TO_SOT_SMD:TO-252-2
- removed U3: 74LVC2G74, Package_SO:TSSOP-8_3x3mm_P0.65mm
- removed U5: NE555D, Package_SO:SOIC-8_3.9x4.9mm_P1.27mm
- removed U6: CD74HC30PWR, Package_SO:TSSOP-14_4.4x5mm_P0.65mm
- removed U7: 4072, Package_SO:TSSOP-14_4.4x5mm_P0.65mm
- removed U8: 4001, Package_SO:SC-74A-5_1.55x2.9mm_P0.95mm
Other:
- board outline removed
- board text added: "Zzzzz |\ _,,,--,,_ /,`.-'`' ._ \-;;,_ |,4- ) )_ .;.( `'-' '---''(_/._)-'(_\_)"
